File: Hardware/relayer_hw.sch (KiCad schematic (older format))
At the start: 57 parts, among them J1 BOOT0, J2 AC_OUT, J3 STLink, J4 AC_IN, Q1 2N7002, SW1 NRST, SW2 USR_SW, U1 STM32WB55, U2 902-9040, U3 LM1117-3.3, Y1 Crystal, Y2 Crystal_GND23

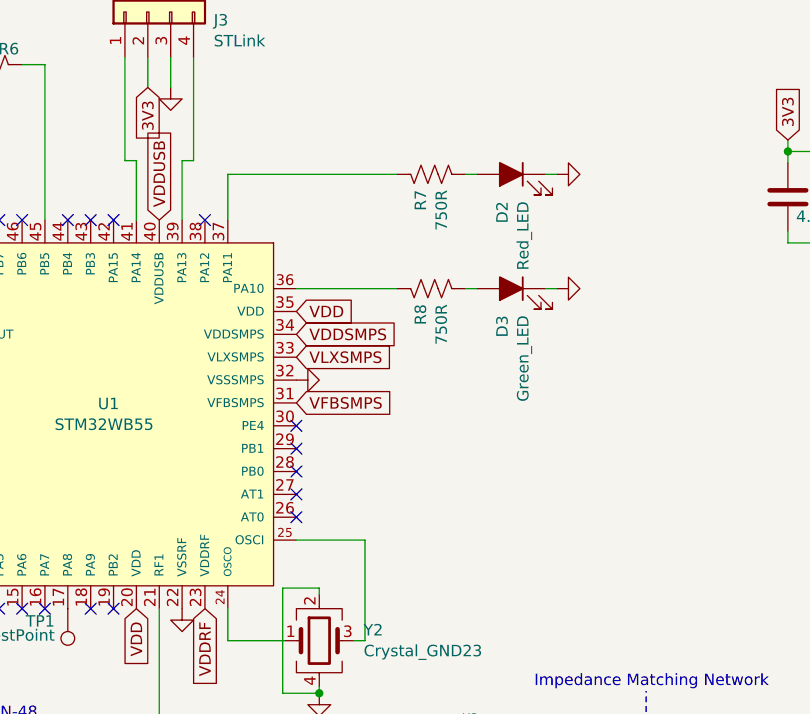
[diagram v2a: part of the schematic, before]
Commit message: Rotas dos caps de desacoplamento/ zonas de cobre externas/ posicionamento de componentes
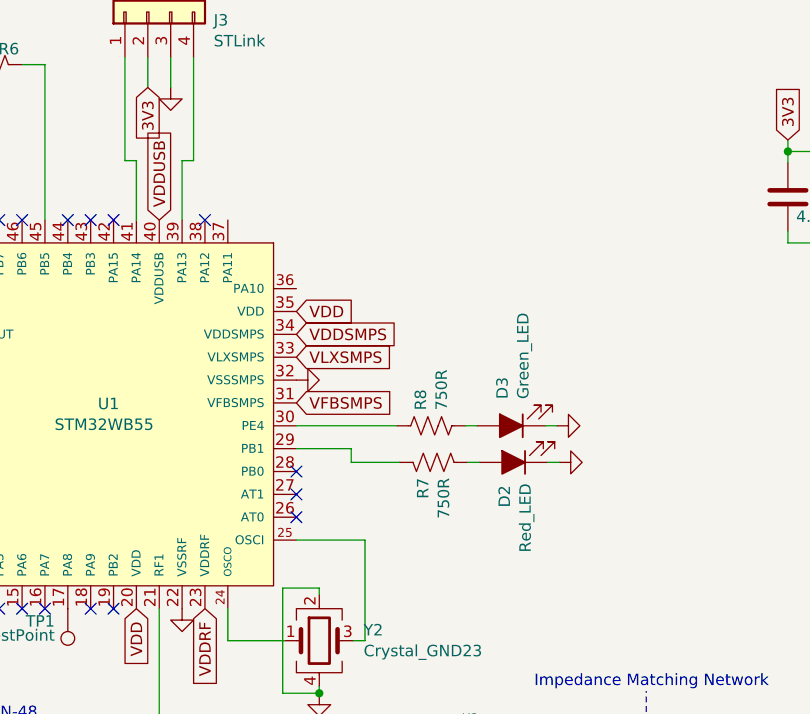
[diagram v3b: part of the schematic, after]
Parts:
- IPD1: footprint Usr_pretty_lib:SON160P500X500X140-6N -> Usr_pretty_lib:MLPF-WB55-01E3
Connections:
- net at U1.29 (PB1): now also R7.1
- net at U1.30 (PE4): now also R8.1
- net at U1.36 (PA10): no longer R8.1
- net at U1.37 (PA11): no longer R7.1
- no-connect marks 22 -> 20
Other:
- moved on the sheet: D2, D3, R7, R8
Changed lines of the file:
@@
 L Device:LED_ALT D2
 U 1 1 60B4B1B5
-P 5200 3130
-F 0 "D2" V 5239 3012 50  0000 R CNN
-F 1 "Red_LED" V 5148 3012 50  0000 R CNN
-F 2 "LED_THT:LED_D5.0mm_Clear" H 5200 3130 50  0001 C CNN
-F 3 "https://www.mouser.com/datasheet/2/239/liteon_LTL2R3KRD-EM-1175128.pdf" H 5200 3130 50  0001 C CNN
-	1    5200 3130
-	-1   0    0    -1
+P 5210 4390
+F 0 "D2" V 5249 4587 50  0000 R CNN
+F 1 "Red_LED" V 5158 4784 50  0000 R CNN
+F 2 "LED_THT:LED_D5.0mm_Clear" H 5210 4390 50  0001 C CNN
+F 3 "https://www.mouser.com/datasheet/2/239/liteon_LTL2R3KRD-EM-1175128.pdf" H 5210 4390 50  0001 C CNN
+	1    5210 4390
+	-1   0    0    1
 $EndComp
 Text GLabel 2670 1620 2    50   Input ~ 0
@@
 $EndComp
 Wire Wire Line
-	5350 3130 5400 3130
+	5360 4390 5410 4390
 $Comp
 L Usr_Sym:STM32WB55 U1
@@
 $EndComp
 Wire Wire Line
-	5000 3130 5050 3130
+	5010 4390 5060 4390
 $Comp
 L Device:C Z1
@@
 F 0 "IPD1" H 4170 6425 50  0000 C CNN
 F 1 "MLPF-WB55-01E3" H 4170 6334 50  0000 C CNN
-F 2 "Usr_pretty_lib:SON160P500X500X140-6N" H 4220 6060 50  0001 C CNN
+F 2 "Usr_pretty_lib:MLPF-WB55-01E3" H 4220 6060 50  0001 C CNN
 F 3 "https://www.st.com/resource/en/datasheet/mlpf-wb55-01e3.pdf" H 4220 6060 50  0001 C CNN
 	1    4220 6060
@@
 	3160 2650 3160 3330
 Wire Wire Line
-	4260 3630 4700 3630
-Wire Wire Line
-	5050 3630 5000 3630
+	4260 4230 4700 4230
+Wire Wire Line
+	5050 4230 5000 4230
 $Comp
 L Device:R_US R8
 U 1 1 609B7C5B
-P 4850 3630
-F 0 "R8" H 4918 3676 50  0000 L CNN
-F 1 "750R" H 4918 3585 50  0000 L CNN
-F 2 "Resistor_SMD:R_0805_2012Metric_Pad1.15x1.40mm_HandSolder" V 4890 3620 50  0001 C CNN
-F 3 "~" H 4850 3630 50  0001 C CNN
-	1    4850 3630
-	0    -1   1    0
-$EndComp
-Wire Wire Line
-	5400 3630 5350 3630
+P 4850 4230
+F 0 "R8" H 4918 4276 50  0000 L CNN
+F 1 "750R" H 4918 4185 50  0000 L CNN
+F 2 "Resistor_SMD:R_0805_2012Metric_Pad1.15x1.40mm_HandSolder" V 4890 4220 50  0001 C CNN
+F 3 "~" H 4850 4230 50  0001 C CNN
+	1    4850 4230
+	0    -1   -1   0
+$EndComp
+Wire Wire Line
+	5400 4230 5350 4230
 $Comp
 L Device:LED_ALT D3
 U 1 1 60B58017
-P 5200 3630
-F 0 "D3" V 5239 3513 50  0000 R CNN
-F 1 "Green_LED" V 5148 3513 50  0000 R CNN
-F 2 "LED_THT:LED_D5.0mm_Clear" H 5200 3630 50  0001 C CNN
-F 3 "https://br.mouser.com/datasheet/2/239/liteon_LTL2R3KGD-EM%20Preliminary-1175478.pdf" H 5200 3630 50  0001 C CNN
-	1    5200 3630
-	-1   0    0    -1
-$EndComp
-Wire Wire Line
-	3960 3330 3960 3130
-Wire Wire Line
-	3960 3130 4700 3130
+P 5200 4230
+F 0 "D3" V 5239 4113 50  0000 R CNN
+F 1 "Green_LED" V 5148 4113 50  0000 R CNN
+F 2 "LED_THT:LED_D5.0mm_Clear" H 5200 4230 50  0001 C CNN
+F 3 "https://br.mouser.com/datasheet/2/239/liteon_LTL2R3KGD-EM%20Preliminary-1175478.pdf" H 5200 4230 50  0001 C CNN
+	1    5200 4230
+	-1   0    0    1
+$EndComp
 Wire Wire Line
 	3660 5030 3660 5960
@@
 L Device:R_US R7
 U 1 1 609AB9F8
-P 4850 3130
-F 0 "R7" H 4918 3176 50  0000 L CNN
-F 1 "750R" H 4918 3085 50  0000 L CNN
-F 2 "Resistor_SMD:R_0805_2012Metric_Pad1.15x1.40mm_HandSolder" V 4890 3120 50  0001 C CNN
-F 3 "~" H 4850 3130 50  0001 C CNN
-	1    4850 3130
+P 4860 4390
+F 0 "R7" H 4928 4436 50  0000 L CNN
+F 1 "750R" H 4928 4345 50  0000 L CNN
+F 2 "Resistor_SMD:R_0805_2012Metric_Pad1.15x1.40mm_HandSolder" V 4900 4380 50  0001 C CNN
+F 3 "~" H 4860 4390 50  0001 C CNN
+	1    4860 4390
 	0    -1   1    0
 $EndComp
@@
 NoConn ~ 4260 4530
 NoConn ~ 4260 4430
-NoConn ~ 4260 4330
-NoConn ~ 4260 4230
 NoConn ~ 3860 3330
 NoConn ~ 3460 3330
@@
 L power:GND #PWR0112
 U 1 1 60C66853
-P 5400 3130
-F 0 "#PWR0112" H 5400 2880 50  0001 C CNN
-F 1 "GND" H 5405 2957 50  0001 C CNN
-F 2 "" H 5400 3130 50  0001 C CNN
-F 3 "" H 5400 3130 50  0001 C CNN
-	1    5400 3130
+P 5410 4390
+F 0 "#PWR0112" H 5410 4140 50  0001 C CNN
+F 1 "GND" H 5415 4217 50  0001 C CNN
+F 2 "" H 5410 4390 50  0001 C CNN
+F 3 "" H 5410 4390 50  0001 C CNN
+	1    5410 4390
 	0    -1   -1   0
 $EndComp
@@
 L power:GND #PWR0113
 U 1 1 60C727AF
-P 5400 3630
-F 0 "#PWR0113" H 5400 3380 50  0001 C CNN
-F 1 "GND" H 5405 3457 50  0001 C CNN
-F 2 "" H 5400 3630 50  0001 C CNN
-F 3 "" H 5400 3630 50  0001 C CNN
-	1    5400 3630
-	0    -1   -1   0
+P 5400 4230
+F 0 "#PWR0113" H 5400 3980 50  0001 C CNN
+F 1 "GND" H 5405 4057 50  0001 C CNN
+F 2 "" H 5400 4230 50  0001 C CNN
+F 3 "" H 5400 4230 50  0001 C CNN
+	1    5400 4230
+	0    -1   1    0
 $EndComp
 $Comp
@@
 Wire Wire Line
 	2300 4730 2560 4730
+Wire Wire Line
+	4710 4390 4500 4390
+Wire Wire Line
+	4500 4390 4500 4330
+Wire Wire Line
+	4500 4330 4260 4330
 $EndSCHEMATC

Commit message: RF via fences
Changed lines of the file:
@@
 P 5460 5760
 F 0 "#PWR0109" H 5460 5510 50  0001 C CNN
-F 1 "GND" H 5465 5587 50  0000 C CNN
+F 1 "GND" H 5465 5587 50  0001 C CNN
 F 2 "" H 5460 5760 50  0001 C CNN
 F 3 "" H 5460 5760 50  0001 C CNN
@@
 P 4580 5760
 F 0 "#PWR0110" H 4580 5510 50  0001 C CNN
-F 1 "GND" H 4585 5587 50  0000 C CNN
+F 1 "GND" H 4585 5587 50  0001 C CNN
 F 2 "" H 4580 5760 50  0001 C CNN
 F 3 "" H 4580 5760 50  0001 C CNN

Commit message: Correçoes de pepinos do DRC
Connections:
- no-connect marks 20 -> 22
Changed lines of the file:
@@
 Wire Wire Line
 	4500 4330 4260 4330
+NoConn ~ 4260 3630
+NoConn ~ 3960 3330
 $EndSCHEMATC

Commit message: Correcao nos capacitores/Revisões de nets
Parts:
- C12, C5: footprint Capacitor_SMD:C_0201_0603Metric -> Capacitor_SMD:C_0402_1005Metric
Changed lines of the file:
@@
 F 0 "C12" H 8375 3276 50  0000 L CNN
 F 1 "4.7μF" H 8296 3145 50  0000 L CNN
-F 2 "Capacitor_SMD:C_0201_0603Metric" H 8298 3080 50  0001 C CNN
+F 2 "Capacitor_SMD:C_0402_1005Metric" H 8298 3080 50  0001 C CNN
 F 3 "https://br.mouser.com/ProductDetail/Samsung-Electro-Mechanics/CL03A475MQ5C65C?qs=sGAEpiMZZMuMW9TJLBQkXnK2T9n4gY42cYfvJEEERh4%3D" H 8260 3230 50  0001 C CNN
 	1    8260 3230
@@
 F 0 "C5" H 6525 3276 50  0000 L CNN
 F 1 "4.7μF" H 6446 3145 50  0000 L CNN
-F 2 "Capacitor_SMD:C_0201_0603Metric" H 6448 3080 50  0001 C CNN
+F 2 "Capacitor_SMD:C_0402_1005Metric" H 6448 3080 50  0001 C CNN
 F 3 "https://br.mouser.com/ProductDetail/Samsung-Electro-Mechanics/CL03A475MQ5C65C?qs=sGAEpiMZZMuMW9TJLBQkXnK2T9n4gY42cYfvJEEERh4%3D" H 6410 3230 50  0001 C CNN
 	1    6410 3230

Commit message: Revisao para especificacoes da JLCPCB
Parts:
- C15: footprint Capacitor_THT:CP_Radial_D5.0mm_P2.00mm -> Usr_pretty_lib:cap_elec
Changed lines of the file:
@@
 F 0 "C15" H 8965 1646 50  0000 L CNN
 F 1 "220μF" H 8965 1555 50  0000 L CNN
-F 2 "Capacitor_THT:CP_Radial_D5.0mm_P2.00mm" H 8850 1600 50  0001 C CNN
+F 2 "Usr_pretty_lib:cap_elec" H 8850 1600 50  0001 C CNN
 F 3 "https://www.mouser.com/datasheet/2/212/KEM_A4055_ESE-1140496.pdf" H 8850 1600 50  0001 C CNN
 	1    8850 1600
